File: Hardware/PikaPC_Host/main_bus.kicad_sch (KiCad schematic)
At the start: 6 parts, among them J2 DIN41612_03x32_C_Split, J3 Conn_01x03, U2 ATF1508AS, U6 74ALVC164245

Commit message: Rework Host Card bus clock
add optional separate bus oscillator
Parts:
- added C54: 100nF, Capacitor_SMD:C_0805_2012Metric, symbol Device:C_Small_US
- added Y3: 25M, Oscillator:Oscillator_DIP-8, symbol Oscillator:CXO_DIP8
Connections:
- net +5V: now also C54.1, Y3.8 (Vcc)
- net BusClk3: now also U2.83 (GCLK1), U6.26 (2A7); no longer J3.2 (Pin_2)
- net CpuClk: now also J3.1 (Pin_1); no longer U6.23 (2B7)
- net GND: now also C54.2, Y3.4 (GND)
- net BusClkDiv3: no longer names the net of U2.45 (IO67)
- net BusClkDiv3: no longer J3.3 (Pin_3)
- removed net CpuClk3: J3.1 (Pin_1), U2.83 (GCLK1), U6.26 (2A7)
- new net BusClk5: J3.2 (Pin_2), U6.23 (2B7)
- new net BusOsc: J3.3 (Pin_3), Y3.5 (OUT)

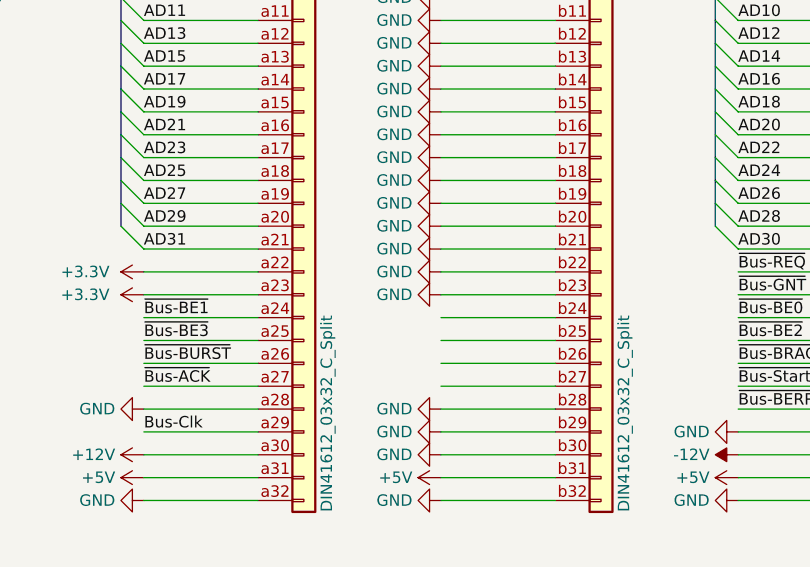
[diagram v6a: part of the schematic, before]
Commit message: Un-assign main bus pins 22 & 23
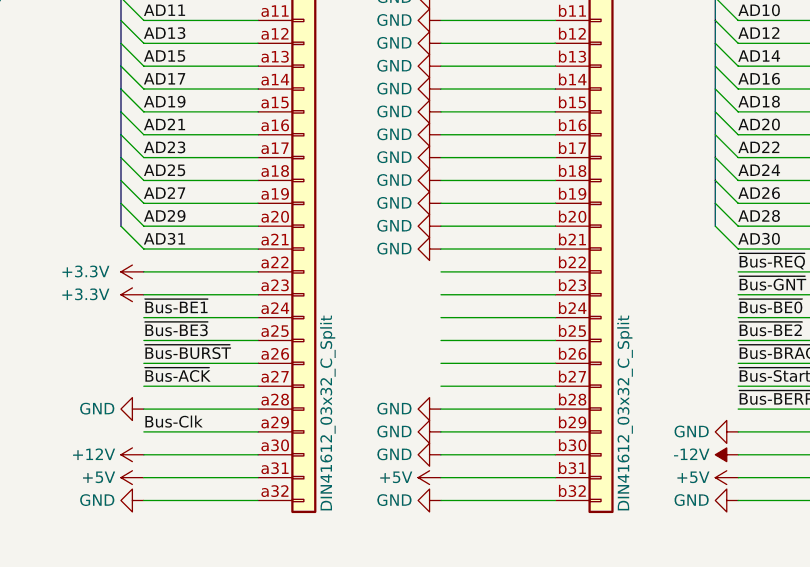
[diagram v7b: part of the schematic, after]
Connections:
- net GND: no longer J2.b22 (Pin_b22), J2.b23 (Pin_b23)
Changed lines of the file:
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@@
-	)
-	(symbol
-		(lib_id "power:GND")
-		(at 208.28 71.12 270)
-		(unit 1)
-		(exclude_from_sim no)
-		(in_bom yes)
-		(on_board yes)
-		(dnp no)
-		(fields_autoplaced yes)
-		(property "Reference" "#PWR0148"
-			(at 201.93 71.12 0)
-			(effects
-				(font
-					(size 1.27 1.27)
-				)
-				(hide yes)
-			)
-		)
-		(property "Value" "GND"
-			(at 205.1051 71.12 90)
-			(effects
-				(font
-					(size 1.27 1.27)
-				)
-				(justify right)
-			)
-		)
-		(property "Footprint" ""
-			(at 208.28 71.12 0)
-			(effects
-				(font
-					(size 1.27 1.27)
-				)
-				(hide yes)
-			)
-		)
-		(property "Datasheet" ""
-			(at 208.28 71.12 0)
-			(effects
-				(font
-					(size 1.27 1.27)
-				)
-				(hide yes)
-			)
-		)
-		(property "Description" "Power symbol creates a global label with name \"GND\" , ground"
-			(at 208.28 71.12 0)
-			(effects
-				(font
-					(size 1.27 1.27)
-				)
-				(hide yes)
-			)
-		)
-		(pin "1"
-		)
-		(instances
-			(project "PikaPC_Host"
-				(path "/6a60ec03-e28d-46ba-8906-3c4e1028fc94/541b8728-35ef-42a9-8317-6c507b38c6a8"
-					(reference "#PWR0148")
-					(unit 1)
-				)
-			)
-		)
 	)
 	(symbol
@@
 					(unit 1)
 				)
-			)
-		)
-	)
-	(symbol
-		(lib_id "power:GND")
-		(at 208.28 73.66 270)
-		(unit 1)
-		(exclude_from_sim no)
-		(in_bom yes)
-		(on_board yes)
-		(dnp no)
-		(fields_autoplaced yes)
-		(property "Reference" "#PWR0149"
-			(at 201.93 73.66 0)
-			(effects
-				(font
-					(size 1.27 1.27)
-				)
-				(hide yes)
-			)
-		)
-		(property "Value" "GND"
-			(at 205.1051 73.66 90)
-			(effects
-				(font
-					(size 1.27 1.27)
-				)
-				(justify right)
-			)
-		)
-		(property "Footprint" ""
-			(at 208.28 73.66 0)
-			(effects
-				(font
-					(size 1.27 1.27)
-				)
-				(hide yes)
-			)
-		)
-		(property "Datasheet" ""
-			(at 208.28 73.66 0)
-			(effects
-				(font
-					(size 1.27 1.27)
-				)
-				(hide yes)
-			)
-		)
-		(property "Description" "Power symbol creates a global label with name \"GND\" , ground"
-			(at 208.28 73.66 0)
-			(effects
-				(font
-					(size 1.27 1.27)
-				)
-				(hide yes)
-			)
-		)
-		(pin "1"
-		)
-		(instances
-			(project "PikaPC_Host"
-				(path "/6a60ec03-e28d-46ba-8906-3c4e1028fc94/541b8728-35ef-42a9-8317-6c507b38c6a8"
-					(reference "#PWR0149")
-					(unit 1)
-				)

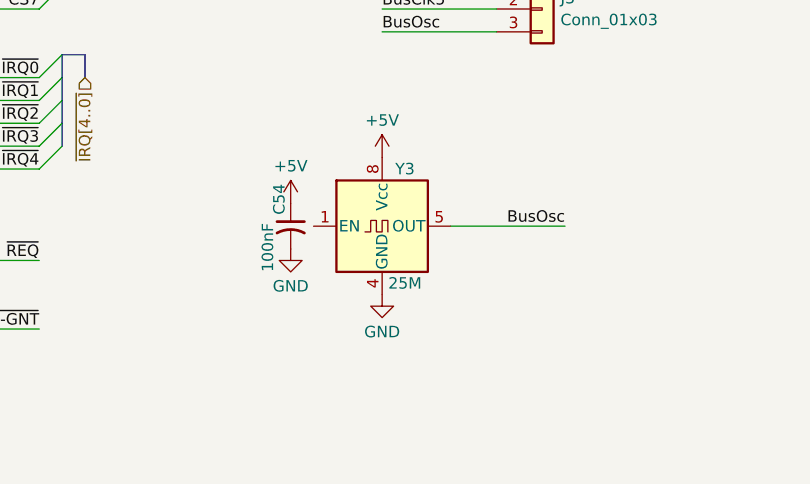
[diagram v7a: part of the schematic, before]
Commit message: Annotate & prep for output - Host & KBC
add gerber output to gitignore
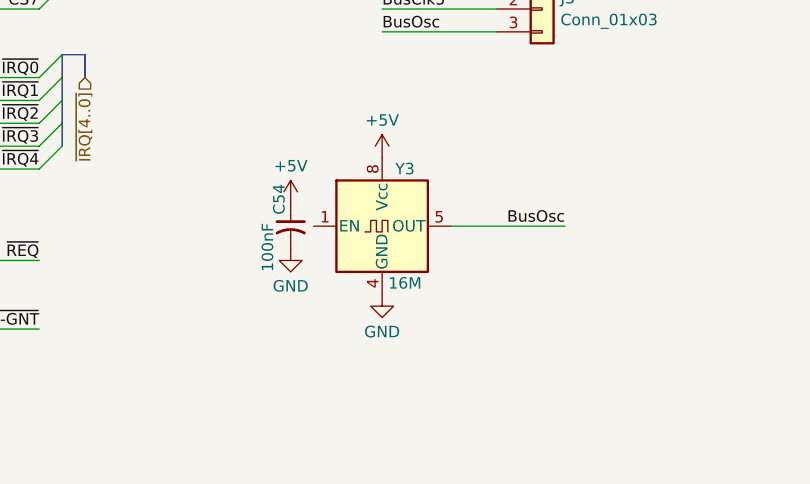
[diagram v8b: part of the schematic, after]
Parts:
- C36, C37, C54: Mouser (none) -> 187-CL21B104KACNNNC
- Y3: value 25M -> 16M
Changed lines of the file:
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@@
 			)
 		)
+		(property "Mouser" "187-CL21B104KACNNNC"
+			(at 119.38 25.4 90)
+			(effects
+				(font
+					(size 1.27 1.27)
+				)
+				(hide yes)
+			)
+		)
 		(pin "2"
 		)
@@
 			)
 		)
+		(property "Mouser" "187-CL21B104KACNNNC"
+			(at 104.14 138.43 90)
+			(effects
+				(font
+					(size 1.27 1.27)
+				)
+				(hide yes)
+			)
+		)
 		(pin "2"
 		)
@@
 			)
 		)
-		(property "Value" "25M"
+		(property "Value" "16M"
 			(at 116.84 144.78 0)
 			(effects
@@
 			(effects
 				(font
+					(size 1.27 1.27)
+				)
+				(hide yes)
+			)
+		)
+		(property "Mouser" "187-CL21B104KACNNNC"
+			(at 132.08 25.4 90)
+			(effects
+				(font
